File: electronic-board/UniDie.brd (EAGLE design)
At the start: 79.6 x 82.8 mm, 24 parts, among them IC1 ATMEGA88-THIN

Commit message: Design schematics for new controller
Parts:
- removed IC1: ATMEGA88-THIN, fab:TQFP32-08THIN
- added U1: ATMEGA328PB-AU, ATMEGA328PB-AU:QFP80P900X900X120-32N
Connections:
- net 5V: now also R14.1, U1.18, U1.4; no longer IC1.18, IC1.4, IC1.6, R14.2
- net GND: now also U1.21, U1.5; no longer IC1.21, IC1.3, IC1.5
- net GT1: now also U1.26; no longer IC1.26
- net GT2: now also U1.25; no longer IC1.25
- net MISO: no longer IC1.16
- net MOSI: no longer IC1.15
- net N$10: now also U1.30; no longer IC1.30
- net N$3: now also U1.28; no longer IC1.28
- net N$4: now also U1.27; no longer IC1.27
- net N$6: now also U1.2; no longer IC1.2
- net N$7: now also U1.1; no longer IC1.1
- net N$8: now also U1.32; no longer IC1.32
- net N$9: now also U1.31; no longer IC1.31
- net RST: now also R14.2, U1.29; no longer IC1.29, R14.1
- net SCK: no longer IC1.17
- net SWT: no longer IC1.14
- net TRM: no longer IC1.10
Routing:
- net N$7: track 31.1 -> 0.00 mm
- net 5V: track 144.1 -> 122.9 mm
- net GND: track 121.8 -> 109.6 mm
- net RST: track 23.3 -> 11.8 mm
- net N$3: track 10.7 -> 0.00 mm
- net N$10: track 7.00 -> 0.00 mm
- net N$9: track 6.22 -> 0.00 mm
- net N$6: track 5.89 -> 0.00 mm
- net N$8: track 5.44 -> 0.00 mm
- net SWT: track 31.1 -> 29.5 mm
- net MOSI: track 21.5 -> 20.0 mm
- net TRM: track 17.5 -> 16.0 mm
- net N$4: track 30.8 -> 29.6 mm
- net MISO: track 11.6 -> 10.5 mm
- net GT1: track 74.8 -> 73.9 mm
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
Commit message: Add thinner traces package for the microcontroller, re-arrange routes. To be finishes
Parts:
- removed U1: ATMEGA328PB-AU, ATMEGA328PB-AU:QFP80P900X900X120-32N
- added U$3: ATMEGA328PB-AU-THIN, AG:TQFP32-08THIN
- moved U$2 0.80 mm to (74.4, 38.8), turned to 270 degrees
- moved U$1 0.40 mm to (56.4, 38.4), turned to 90 degrees
- turned R14 to 270 degrees
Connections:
- net 5V: now also U$3.18, U$3.4; no longer U1.18, U1.4
- net GND: now also U$3.21, U$3.5; no longer U1.21, U1.5
- net GT1: now also U$3.26; no longer U1.26
- net GT2: now also U$3.25; no longer U1.25
- net MISO: now also U$3.23
- net MOSI: now also U$3.22
- net N$10: now also U$3.30; no longer U1.30
- net N$3: now also U$3.28; no longer U1.28
- net N$4: now also U$3.27; no longer U1.27
- net N$6: now also U$3.2; no longer U1.2
- net N$7: now also U$3.1; no longer U1.1
- net N$8: now also U$3.32; no longer U1.32
- net N$9: now also U$3.31; no longer U1.31
- net RST: now also U$3.29; no longer U1.29
- net SCK: now also U$3.24
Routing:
- net RST: track 11.8 -> 33.0 mm
- net MOSI: track 20.0 -> 8.52 mm
- net N$3: track 0.00 -> 11.0 mm
- net 5V: track 122.9 -> 130.7 mm
- net N$10: track 0.00 -> 7.40 mm
- net N$9: track 0.00 -> 6.74 mm
- net MISO: track 10.5 -> 4.44 mm
- net N$8: track 0.00 -> 5.88 mm
- net GND: track 109.6 -> 104.6 mm
- net TRM: track 16.0 -> 14.3 mm
- net SCK: track 8.40 -> 9.97 mm
- net N$1: track 61.2 -> 59.7 mm
- net N$4: track 29.6 -> 31.1 mm
- net GT1: track 73.9 -> 75.2 mm
- net GT2: track 93.5 -> 94.5 mm

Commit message: Find a board layout apt for 328pb
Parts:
- moved R14 40.9 mm to (29.6, 58.0), turned to 0 degrees
- moved R7 3.94 mm to (70.0, 50.3)
- moved R4 1.65 mm to (43.6, 48.4)
- moved R2 1.60 mm to (29.6, 60.8), turned to 0 degrees
- moved R8 1.13 mm to (57.6, 49.2)
- moved R15 0.89 mm to (57.2, 44.8)
- moved PNP2 0.40 mm to (34.8, 63.6)
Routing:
- net RST: track 33.0 -> 168.2 mm
- net 5V: track 130.7 -> 84.0 mm
- net N$7: track 0.00 -> 31.5 mm
- net N$11: track 9.93 -> 0.00 mm
- net N$12: track 8.99 -> 0.00 mm
- net N$4: track 31.1 -> 23.2 mm
- net GT2: track 94.5 -> 87.9 mm
- net GND: track 104.6 -> 110.6 mm
- net GT1: track 75.2 -> 69.7 mm
- net N$6: track 0.00 -> 5.16 mm
- net SEG6: track 48.2 -> 45.2 mm
- net N$3: track 11.0 -> 9.00 mm
- net SEG2: track 31.5 -> 33.2 mm
- net SEG4: track 27.7 -> 29.4 mm
- net DIG2: track 20.1 -> 18.5 mm
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
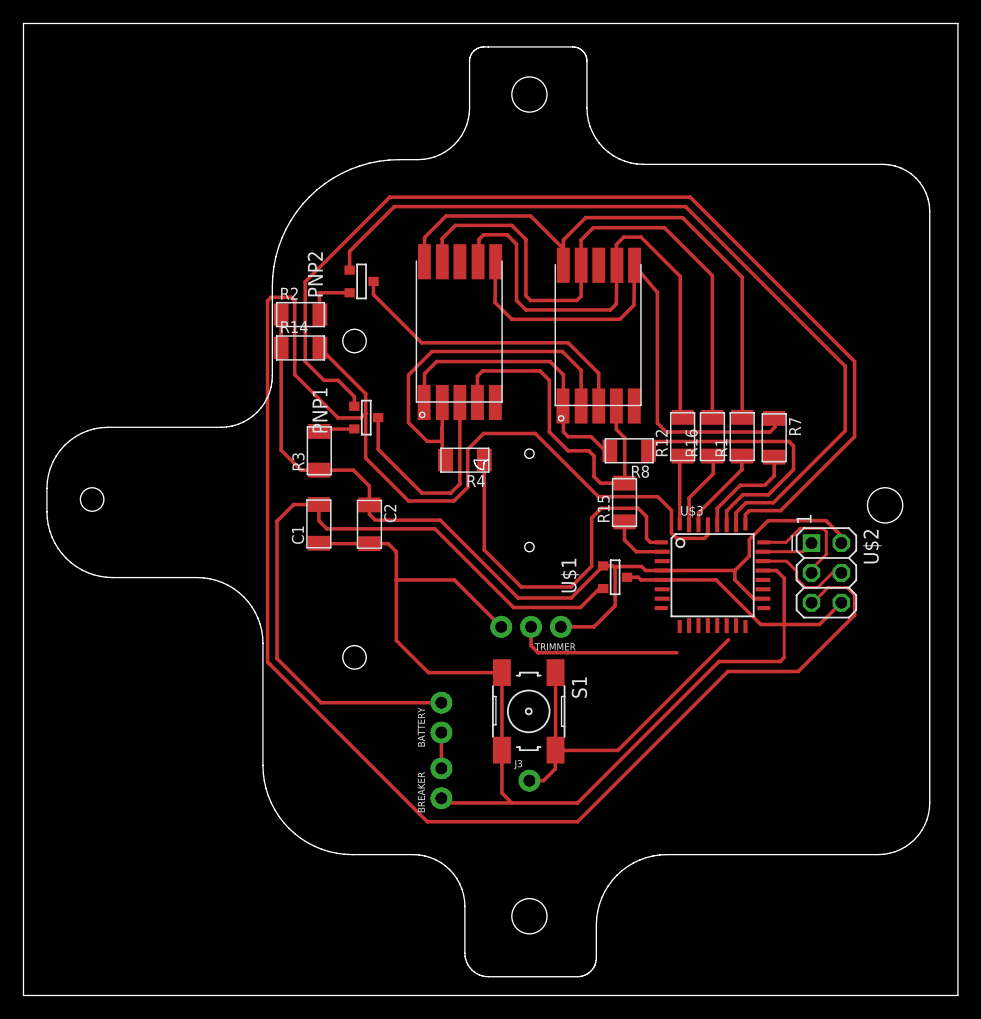
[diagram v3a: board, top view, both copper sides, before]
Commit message: Adjust all routes. Adjust trimmer holes. Adjust outline
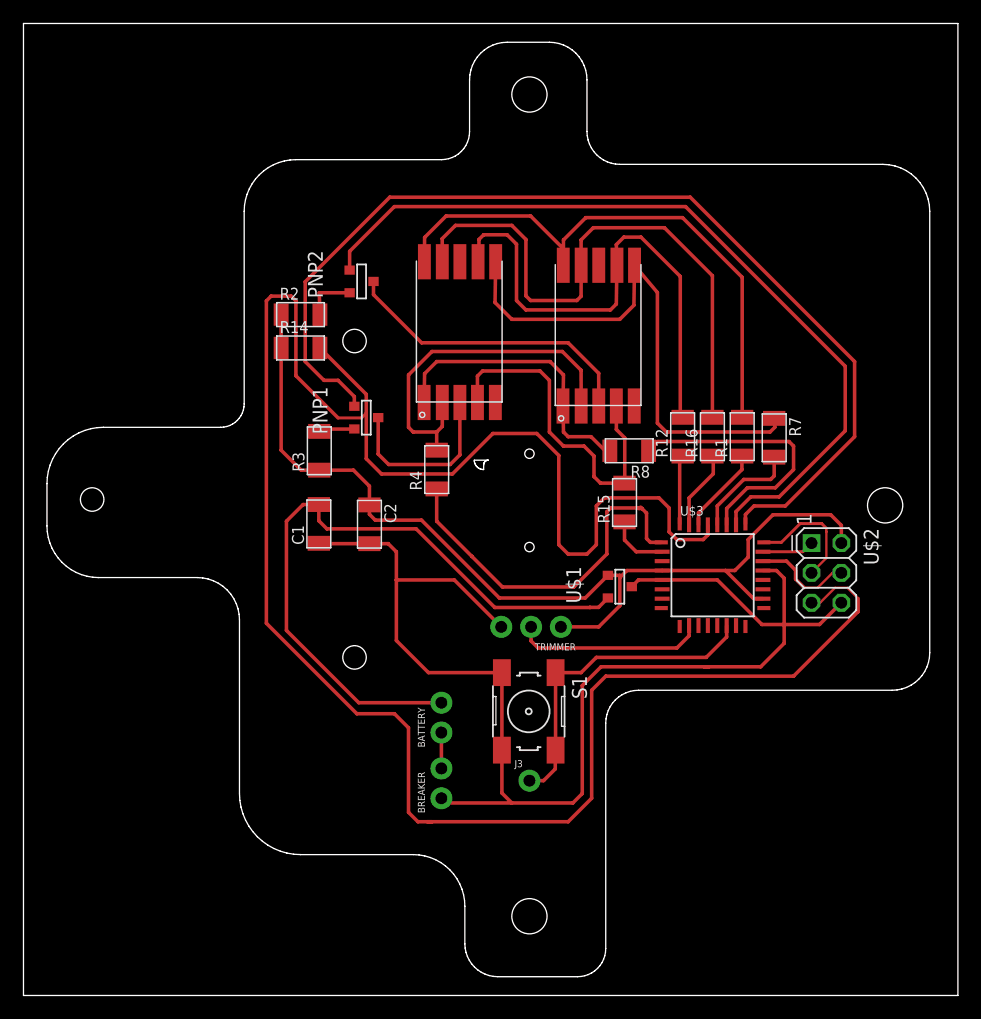
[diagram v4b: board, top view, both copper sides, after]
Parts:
- moved R4 2.53 mm to (41.2, 47.6), turned to 90 degrees
- moved U$1 0.89 mm to (56.8, 37.6)
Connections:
- net SWT: now also U$3.14
- net TRM: now also U$3.10
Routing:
- net RST: track 168.2 -> 183.6 mm
- net GND: track 110.6 -> 115.5 mm
- net DIG2: track 18.5 -> 15.2 mm
- net N$1: track 60.7 -> 57.8 mm
- net SEG2: track 33.2 -> 30.5 mm
- net TRM: track 14.3 -> 16.2 mm
- net SWT: track 29.5 -> 27.6 mm
- net 5V: track 84.0 -> 84.8 mm
- net SCK: track 9.97 -> 10.5 mm
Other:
- outline, holes or cut-outs redrawn
